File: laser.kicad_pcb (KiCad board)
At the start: 4 copper layers, 90.2 x 50.9 mm, 124 parts, among them IC201 ADM7172ACPZ-4.2-R7, IC202 LT1716CS5#TRPBF, IC203 ADM7154ARDZ-3.3-R7, IC204 IRF9358PBF, IC601 ATMEGA328P-AU, IC602 FT232RL-TUBE, IC701 MAX6126AASA25+, IC801 ADS122C04IPWR, J601 M20-9980345, J602 USB_Connector, Q401 RSR030N06TL, U101 281698-3, U201 LM4040EIM3X-2.5_NOPB, U301 OPA569AIDWPR, U302 OPA569AIDWPR, U401 ADA4528-2ACPZ-RL, U402 782853152_WE-CBA_08, U501 ADA4528-2ACPZ-RL, U502 ADA4528-2ACPZ-RL, U801 MAX5217GUA+, U802 MAX5217GUA+, Y601 ECS-160-16-33B-CKM-TR

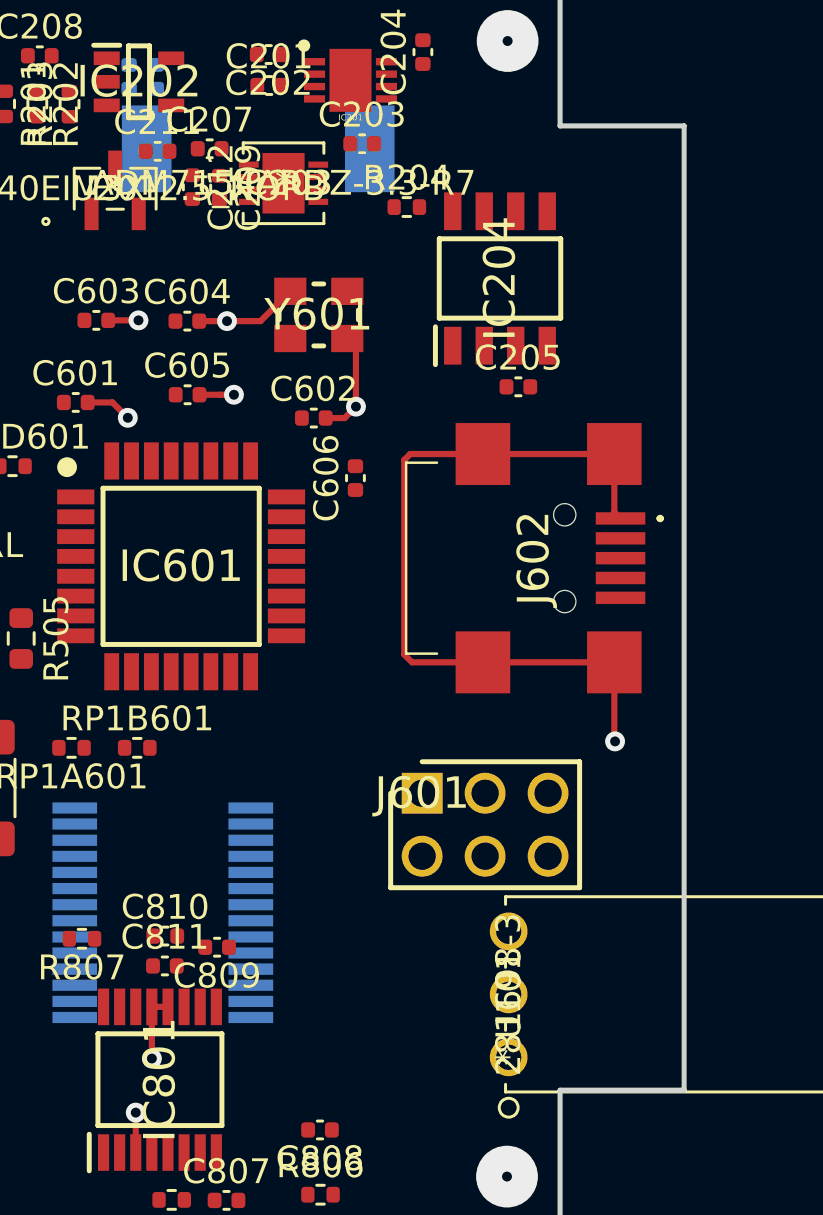
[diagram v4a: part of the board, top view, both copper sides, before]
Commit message: added grounds, finished 5v ext trace
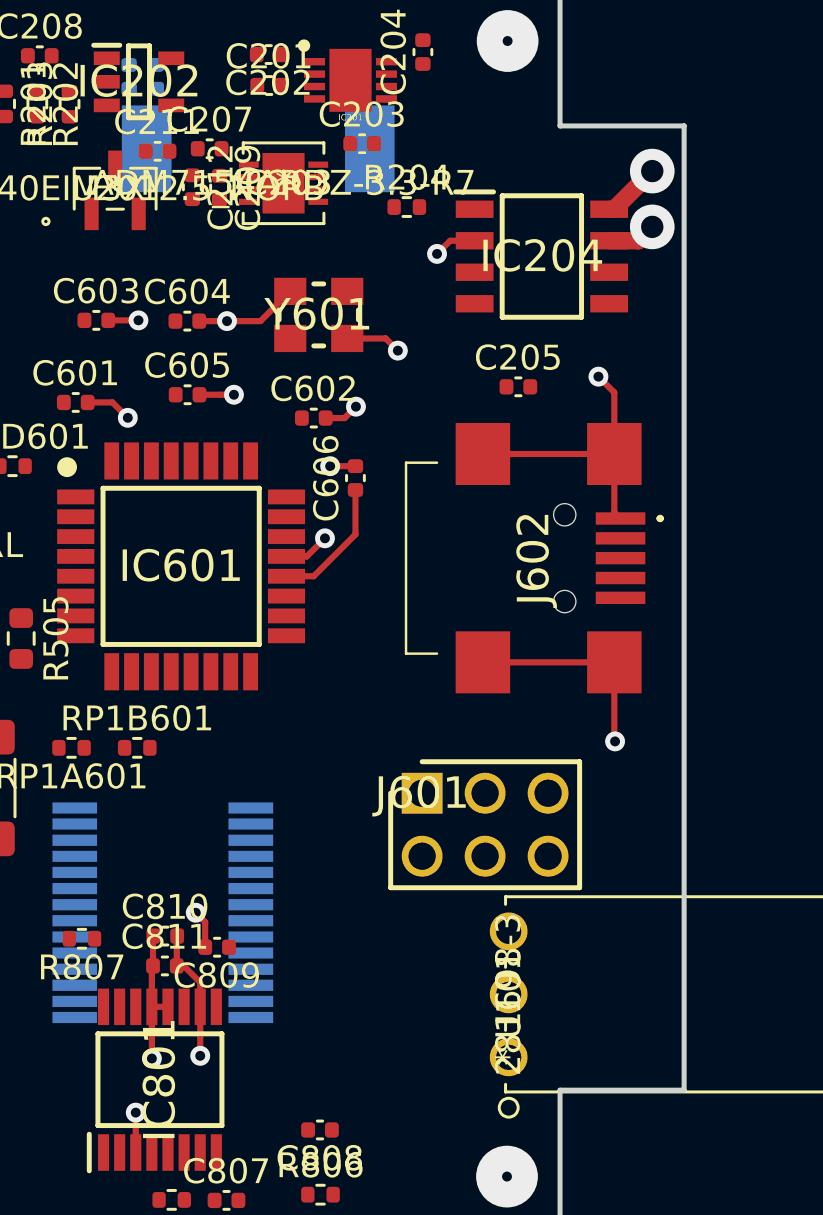
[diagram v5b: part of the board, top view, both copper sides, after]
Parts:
- moved IC204 1.91 mm to (207.2, 92.6), turned to 0 degrees
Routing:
- net 5V_EXTERNAL_Power_Source: track 31.5 -> 40.6 mm, vias 0 -> 2
- net Net-(C606-Pad1): track 0.00 -> 5.27 mm
- net 3.3V: track 4.35 -> 7.22 mm
- net GND: track 204.3 -> 204.7 mm, vias 37 -> 44
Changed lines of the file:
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@@
     (thickness 1.6)
     (drawings 17)
-    (tracks 194)
+    (tracks 237)
     (zones 0)
     (modules 124)
@@
   )
   (setup
-    (last_trace_width 1.8)
+    (last_trace_width 0.25)
     (user_trace_width 0.5)
+    (user_trace_width 0.7)
     (user_trace_width 1.8)
     (trace_clearance 0.2)
@@
     (mod_text_size 1 1)
     (mod_text_width 0.15)
-    (pad_size 0.508 0.508)
-    (pad_drill 0.254)
+    (pad_size 0.7 1.525)
+    (pad_drill 0)
     (pad_to_mask_clearance 0)
     (aux_axis_origin 0 0)
@@
   )
   (module "footprint libraries:IRF9358PBF" (layer F.Cu)
-    (at 205.56 93.48 90)
+    (at 207.248 92.595)
     (descr SO-8-A)
     (tags "Integrated Circuit")
     (attr smd)
-    (fp_text reference IC204 (at 0 0 90) (layer F.SilkS)
+    (fp_text reference IC204 (at 0 0) (layer F.SilkS)
       (effects (font (size 1.27 1.27) (thickness 0.254)))
     )
-    (fp_text value IRF9358PBF (at 0 0 90) (layer F.SilkS) hide
+    (fp_text value IRF9358PBF (at 0 0) (layer F.SilkS) hide
       (effects (font (size 1.27 1.27) (thickness 0.254)))
     )
@@
     (fp_line (start -1.6 2.45) (end -1.6 -2.45) (layer F.SilkS) (width 0.2))
     (fp_line (start -3.475 -2.605) (end -1.95 -2.605) (layer F.SilkS) (width 0.2))
-    (fp_text user %R (at 0 0 90) (layer F.Fab)
+    (fp_text user %R (at 0 0) (layer F.Fab)
       (effects (font (size 1.27 1.27) (thickness 0.254)))
     )
-    (pad 1 smd rect (at -2.712 -1.905 180) (size 0.7 1.525) (layers F.Cu F.Paste F.Mask)
+    (pad 1 smd rect (at -2.712 -1.905 90) (size 0.7 1.525) (layers F.Cu F.Paste F.Mask)
       (net 13 "Net-(C205-Pad1)"))
-    (pad 2 smd rect (at -2.712 -0.635 180) (size 0.7 1.525) (layers F.Cu F.Paste F.Mask)
+    (pad 2 smd rect (at -2.712 -0.635 90) (size 0.7 1.525) (layers F.Cu F.Paste F.Mask)
       (net 119 GND))
-    (pad 3 smd rect (at -2.712 0.635 180) (size 0.7 1.525) (layers F.Cu F.Paste F.Mask)
+    (pad 3 smd rect (at -2.712 0.635 90) (size 0.7 1.525) (layers F.Cu F.Paste F.Mask)
       (net 13 "Net-(C205-Pad1)"))
-    (pad 4 smd rect (at -2.712 1.905 180) (size 0.7 1.525) (layers F.Cu F.Paste F.Mask)
+    (pad 4 smd rect (at -2.712 1.905 90) (size 0.7 1.525) (layers F.Cu F.Paste F.Mask)
       (net 14 "Net-(C205-Pad2)"))
-    (pad 5 smd rect (at 2.712 1.905 180) (size 0.7 1.525) (layers F.Cu F.Paste F.Mask)
+    (pad 5 smd rect (at 2.712 1.905 90) (size 0.7 1.525) (layers F.Cu F.Paste F.Mask)
       (net 16 5.0V))
-    (pad 6 smd rect (at 2.712 0.635 180) (size 0.7 1.525) (layers F.Cu F.Paste F.Mask)
+    (pad 6 smd rect (at 2.712 0.635 90) (size 0.7 1.525) (layers F.Cu F.Paste F.Mask)
       (net 16 5.0V))
-    (pad 7 smd rect (at 2.712 -0.635 180) (size 0.7 1.525) (layers F.Cu F.Paste F.Mask)
+    (pad 7 smd rect (at 2.712 -0.635 90) (size 0.7 1.525) (layers F.Cu F.Paste F.Mask)
       (net 40 5V_EXTERNAL_Power_Source))
-    (pad 8 smd rect (at 2.712 -1.905 180) (size 0.7 1.525) (layers F.Cu F.Paste F.Mask)
+    (pad 8 smd rect (at 2.712 -1.905 90) (size 0.7 1.525) (layers F.Cu F.Paste F.Mask)
       (net 40 5V_EXTERNAL_Power_Source))
     (model IRF9358PBF.stp
@@
   (segment (start 190.87 127.12) (end 190.87 127.12) (width 0.25) (layer F.Cu) (net 7))
   (via (at 190.87 127.12) (size 0.8) (drill 0.4) (layers F.Cu B.Cu) (net 7))
+  (segment (start 191.52 121.250002) (end 191.565001 121.205001) (width 0.25) (layer F.Cu) (net 7))
+  (segment (start 191.52 122.854) (end 191.52 121.250002) (width 0.25) (layer F.Cu) (net 7))
+  (segment (start 191.565001 120.014999) (end 191.58 120) (width 0.25) (layer F.Cu) (net 7))
+  (segment (start 191.565001 121.205001) (end 191.565001 120.014999) (width 0.25) (layer F.Cu) (net 7))
+  (segment (start 198.043002 105.49) (end 196.95 105.49) (width 0.25) (layer F.Cu) (net 33))
+  (segment (start 199.73 103.803002) (end 198.043002 105.49) (width 0.25) (layer F.Cu) (net 33))
+  (segment (start 199.73 102.01) (end 199.73 103.803002) (width 0.25) (layer F.Cu) (net 33))
   (segment (start 211.700001 117.637629) (end 211.700001 93.830001) (width 1.8) (layer PWR) (net 40))
   (segment (start 206.98763 122.35) (end 211.700001 117.637629) (width 1.8) (layer PWR) (net 40))
   (segment (start 205.91 122.35) (end 206.98763 122.35) (width 1.8) (layer PWR) (net 40))
+  (segment (start 211.700001 93.830001) (end 211.700001 93.830001) (width 1.8) (layer PWR) (net 40))
+  (segment (start 211.700001 93.830001) (end 211.700001 92.889999) (width 1.8) (layer PWR) (net 40))
+  (segment (start 211.700001 89.149999) (end 211.700001 89.149999) (width 1.8) (layer PWR) (net 40))
+  (via (at 211.700001 89.149999) (size 1.8) (drill 0.9) (layers F.Cu B.Cu) (net 40))
+  (segment (start 210.16 90.69) (end 211.700001 89.149999) (width 0.7) (layer F.Cu) (net 40))
+  (segment (start 209.96 90.69) (end 210.16 90.69) (width 0.7) (layer F.Cu) (net 40))
+  (segment (start 211.700001 92.889999) (end 211.700001 91.399999) (width 1.8) (layer PWR) (net 40))
+  (segment (start 211.700001 91.399999) (end 211.700001 89.149999) (width 1.8) (layer PWR) (net 40))
+  (via (at 211.700001 91.399999) (size 1.8) (drill 0.9) (layers F.Cu B.Cu) (net 40))
+  (segment (start 211.14 91.96) (end 211.700001 91.399999) (width 0.7) (layer F.Cu) (net 40))
+  (segment (start 209.96 91.96) (end 211.14 91.96) (width 0.7) (layer F.Cu) (net 40))
   (via (at 126.2634 93.2256) (size 2.4892) (drill 0.4) (layers F.Cu B.Cu) (net 119))
   (via (at 130.8354 83.9292) (size 2.4892) (drill 0.4) (layers F.Cu B.Cu) (net 119))
@@
   (segment (start 210.17 108.96) (end 204.87 108.96) (width 0.25) (layer F.Cu) (net 119))
   (segment (start 210.17 100.56) (end 204.87 100.56) (width 0.25) (layer F.Cu) (net 119))
-  (segment (start 204.87 100.56) (end 201.94 100.56) (width 0.25) (layer F.Cu) (net 119))
-  (segment (start 201.94 100.56) (end 201.7 100.8) (width 0.25) (layer F.Cu) (net 119))
-  (segment (start 201.7 100.8) (end 201.7 108.65) (width 0.25) (layer F.Cu) (net 119))
-  (segment (start 202.01 108.96) (end 204.87 108.96) (width 0.25) (layer F.Cu) (net 119))
-  (segment (start 201.7 108.65) (end 202.01 108.96) (width 0.25) (layer F.Cu) (net 119))
   (segment (start 210.17 102.91) (end 210.42 103.16) (width 0.25) (layer F.Cu) (net 119))
   (segment (start 210.17 100.56) (end 210.17 102.91) (width 0.25) (layer F.Cu) (net 119))
@@
   (via (at 199.75 98.65) (size 0.8) (drill 0.4) (layers F.Cu B.Cu) (net 119))
   (segment (start 199.75 96.25) (end 199.4 95.9) (width 0.25) (layer F.Cu) (net 119))
-  (segment (start 199.75 98.65) (end 199.75 96.25) (width 0.25) (layer F.Cu) (net 119))
   (segment (start 188.93 98.48) (end 189.93 98.48) (width 0.25) (layer F.Cu) (net 119))
   (segment (start 189.93 98.48) (end 190.55 99.1) (width 0.25) (layer F.Cu) (net 119))
@@
   (segment (start 171.875 86.1137) (end 171.875 87.598699) (width 0.5) (layer F.Cu) (net 119))
   (segment (start 167.735 108.332) (end 166.465 108.332) (width 0.25) (layer F.Cu) (net 119))
+  (segment (start 204.536 91.96) (end 203.55 91.96) (width 0.25) (layer F.Cu) (net 119))
+  (segment (start 203.55 91.96) (end 203.02 92.49) (width 0.25) (layer F.Cu) (net 119))
+  (segment (start 203.02 92.49) (end 203.02 92.49) (width 0.25) (layer F.Cu) (net 119))
+  (via (at 203.02 92.49) (size 0.8) (drill 0.4) (layers F.Cu B.Cu) (net 119))
+  (segment (start 210.17 100.56) (end 210.17 98.08) (width 0.25) (layer F.Cu) (net 119))
+  (segment (start 210.17 98.08) (end 209.53 97.44) (width 0.25) (layer F.Cu) (net 119))
+  (segment (start 209.53 97.44) (end 209.53 97.44) (width 0.25) (layer F.Cu) (net 119))
+  (via (at 209.53 97.44) (size 0.8) (drill 0.4) (layers F.Cu B.Cu) (net 119))
+  (segment (start 199.73 101.05) (end 198.71 101.05) (width 0.25) (layer F.Cu) (net 119))
+  (segment (start 198.71 101.05) (end 198.71 101.05) (width 0.25) (layer F.Cu) (net 119))
+  (via (at 198.71 101.05) (size 0.8) (drill 0.4) (layers F.Cu B.Cu) (net 119))
+  (segment (start 199.4 95.9) (end 200.95 95.9) (width 0.25) (layer F.Cu) (net 119))
+  (segment (start 200.95 95.9) (end 201.44 96.39) (width 0.25) (layer F.Cu) (net 119))
+  (segment (start 201.44 96.39) (end 201.44 96.39) (width 0.25) (layer F.Cu) (net 119))
+  (via (at 201.44 96.39) (size 0.8) (drill 0.4) (layers F.Cu B.Cu) (net 119))
+  (segment (start 196.95 104.69) (end 197.77 104.69) (width 0.25) (layer F.Cu) (net 119))
+  (segment (start 197.77 104.69) (end 198.5 103.96) (width 0.25) (layer F.Cu) (net 119))
+  (segment (start 198.5 103.96) (end 198.5 103.96) (width 0.25) (layer F.Cu) (net 119))
+  (via (at 198.5 103.96) (size 0.8) (drill 0.4) (layers F.Cu B.Cu) (net 119))
+  (segment (start 192.808501 121.205001) (end 192.525001 121.205001) (width 0.25) (layer F.Cu) (net 119))
+  (segment (start 193.47 121.8665) (end 192.808501 121.205001) (width 0.25) (layer F.Cu) (net 119))
+  (segment (start 193.47 122.854) (end 193.47 121.8665) (width 0.25) (layer F.Cu) (net 119))
+  (segment (start 192.525001 120.014999) (end 192.54 120) (width 0.25) (layer F.Cu) (net 119))
+  (segment (start 192.525001 121.205001) (end 192.525001 120.014999) (width 0.25) (layer F.Cu) (net 119))
+  (segment (start 193.67 120.45) (end 193.67 119.44) (width 0.25) (layer F.Cu) (net 119))
+  (segment (start 193.67 119.44) (end 193.29 119.06) (width 0.25) (layer F.Cu) (net 119))
+  (segment (start 193.29 119.06) (end 193.29 119.06) (width 0.25) (layer F.Cu) (net 119))
+  (via (at 193.29 119.06) (size 0.8) (drill 0.4) (layers F.Cu B.Cu) (net 119))
+  (segment (start 193.47 122.854) (end 193.47 124.83) (width 0.25) (layer F.Cu) (net 119))
+  (segment (start 193.47 124.83) (end 193.47 124.83) (width 0.25) (layer F.Cu) (net 119))
+  (via (at 193.47 124.83) (size 0.8) (drill 0.4) (layers F.Cu B.Cu) (net 119))
   (zone (net 119) (net_name GND) (layer GND) (hatch edge 0.508)
     (priority 1)

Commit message: update netlist from current QA
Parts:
- C408: value 10u -> 0.01u
- moved R407 1.01 mm to (151.0, 127.3), turned to 180 degrees

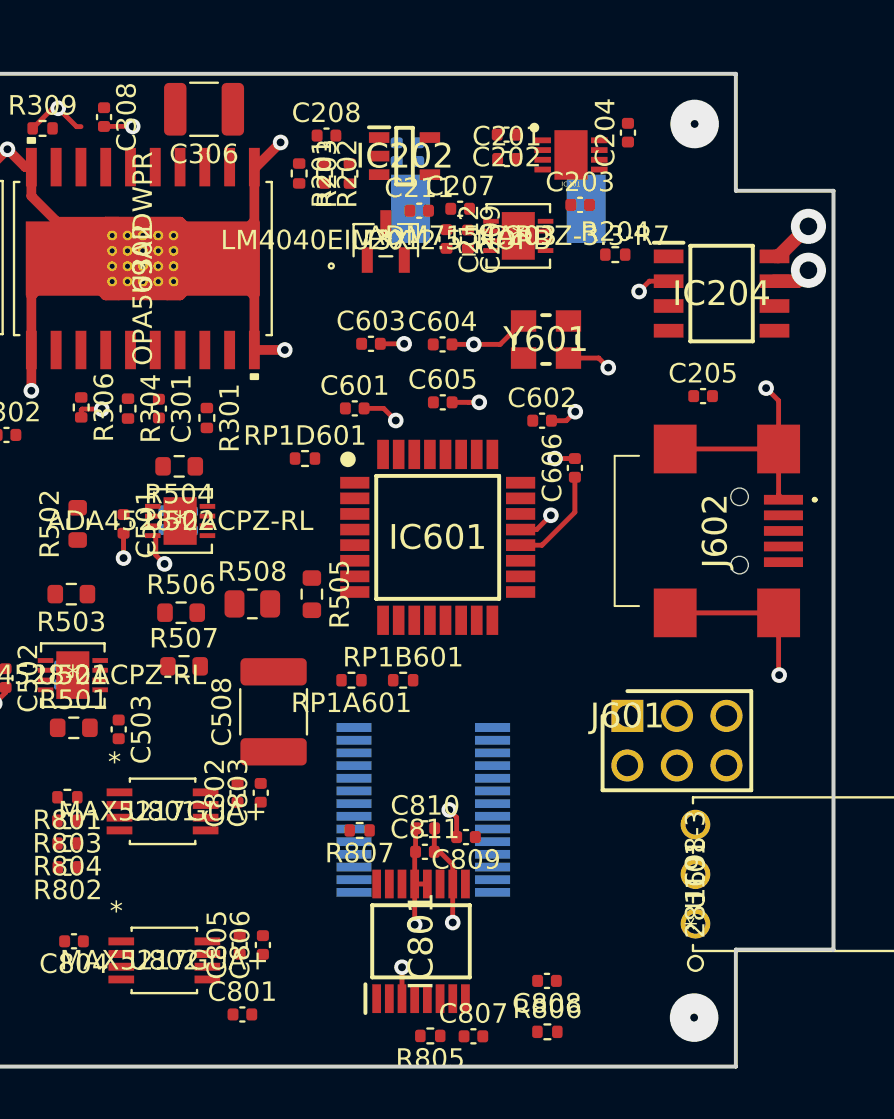
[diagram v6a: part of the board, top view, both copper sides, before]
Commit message: added more traces, plus a few grounds. vias on epads as well
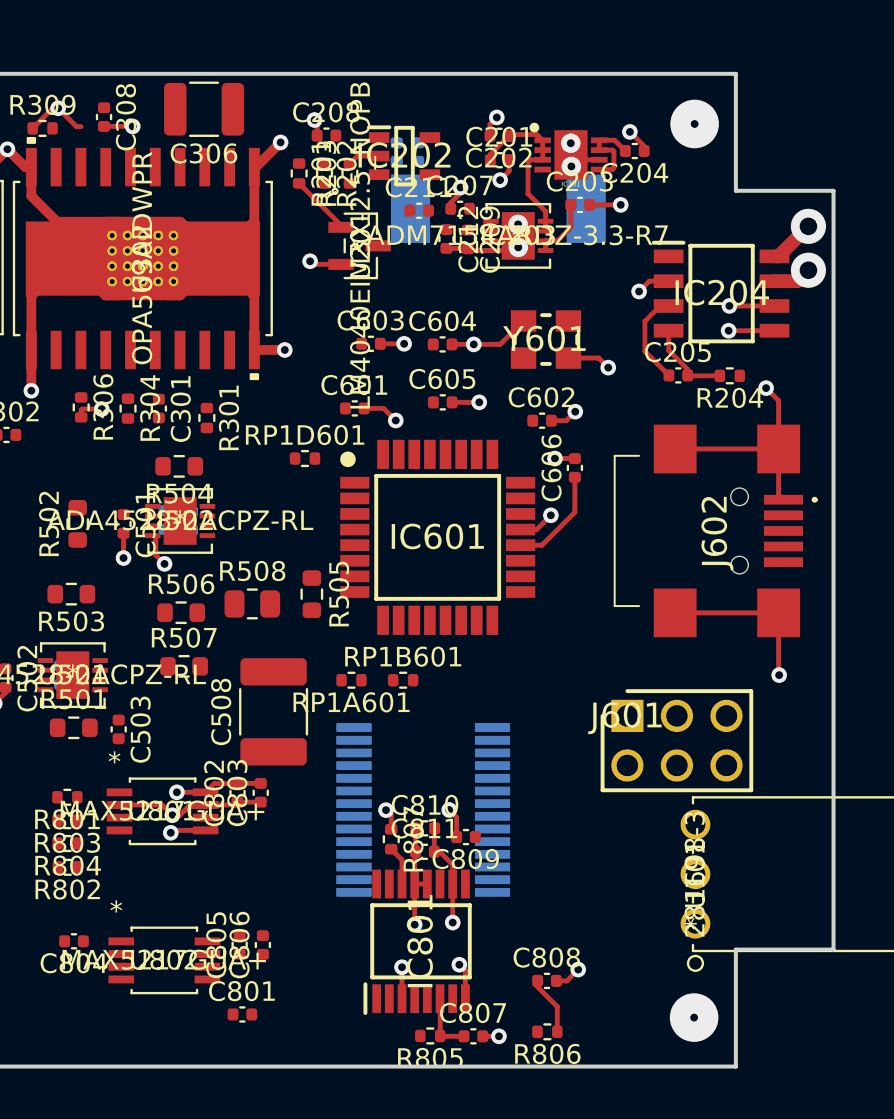
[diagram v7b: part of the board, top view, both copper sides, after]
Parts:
- moved R204 8.55 mm to (207.7, 96.8), turned to 180 degrees
- moved R807 1.68 mm to (190.3, 120.6), turned to 270 degrees
- moved C205 1.65 mm to (205.0, 96.8)
- moved U201 1.31 mm to (188.8, 90.2), turned to 270 degrees
- moved C204 1.00 mm to (202.8, 85.3), turned to 180 degrees
- moved C201 0.37 mm to (195.9, 85.8)
- moved C202 0.37 mm to (195.9, 84.5)
- turned C808 to 0 degrees
- turned R806 to 180 degrees
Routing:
- net GND: track 204.7 -> 229.4 mm, vias 44 -> 59
- net 3.3V: track 7.22 -> 17.9 mm, vias 2 -> 5
- net 4.2V: track 0.00 -> 9.25 mm
- net Net-(C205-Pad1): track 0.00 -> 4.82 mm
- net 5.0V: track 0.00 -> 4.66 mm, vias 0 -> 2
- net Net-(C204-Pad2): track 0.00 -> 4.47 mm
- net Net-(C205-Pad2): track 0.00 -> 4.35 mm
- net Net-(C203-Pad1): track 0.00 -> 3.23 mm
- net Net-(C807-Pad1): track 0.00 -> 3.14 mm
- net Net-(IC202-Pad4): track 0.00 -> 3.14 mm
- net REFERENCE_2.5V: track 0.00 -> 3.03 mm
- net Net-(IC801-Pad14): track 0.00 -> 2.01 mm
